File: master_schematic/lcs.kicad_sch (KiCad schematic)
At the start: 6 parts, among them U10 HX711, U11 HX711, U12 LoadCell, U13 HX711, U14 LoadCell, U3 LoadCell

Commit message: minor updates
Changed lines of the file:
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@@
-		)
-	)
-	(bus
-		(pts
-			(xy 67.31 129.54) (xy 67.31 135.89)
-		)
-		(stroke
-			(width 0)
-			(type default)
 		)
 	)

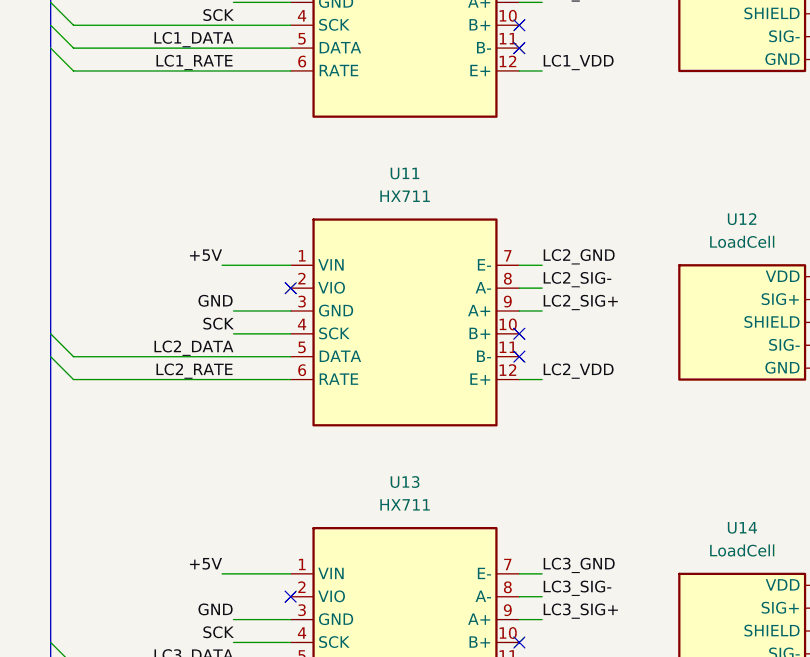
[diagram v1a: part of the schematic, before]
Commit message: updated with part info
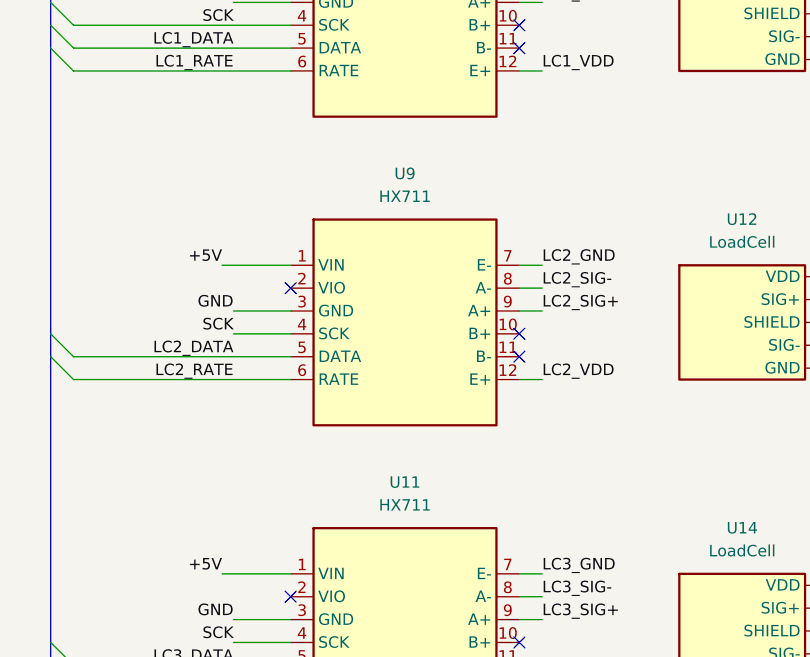
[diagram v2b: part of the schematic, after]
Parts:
- removed U13: HX711, Connector_PinHeader_1.00mm:PinHeader_1x06_P1.00mm_Vertical, symbol hb_symbol_lib:hx711_load_cell_amplifier
- added U9: HX711, hb_footprint_lib:hx711_connector, symbol hb_symbol_lib:hx711_load_cell_amplifier
- U10, U11: footprint Connector_PinHeader_1.00mm:PinHeader_1x06_P1.00mm_Vertical -> hb_footprint_lib:hx711_connector
- U12, U14, U3: now left out of the parts list
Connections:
- net +5V: now also U9.1 (VIN)
- net GND: now also U9.3 (GND)
- net LC2_DATA: now also U9.5 (DATA); no longer U11.5 (DATA)
- net LC2_GND: now also U9.7 (E-); no longer U11.7 (E-)
- net LC2_RATE: now also U9.6 (RATE); no longer U11.6 (RATE)
- net LC2_SIG+: now also U9.9 (A+); no longer U11.9 (A+)
- net LC2_SIG-: now also U9.8 (A-); no longer U11.8 (A-)
- net LC2_VDD: now also U9.12 (E+); no longer U11.12 (E+)
- net LC3_DATA: now also U11.5 (DATA)
- net LC3_GND: now also U11.7 (E-)
- net LC3_RATE: now also U11.6 (RATE)
- net LC3_SIG+: now also U11.9 (A+)
- net LC3_SIG-: now also U11.8 (A-)
- net LC3_VDD: now also U11.12 (E+)
- net SCK: now also U9.4 (SCK)

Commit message: fixed errors on schematic
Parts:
- renumbered U9 to U10, U3 to U12, U12 to U13, U10 to U9
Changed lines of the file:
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@@
 		(dnp no)
 		(fields_autoplaced yes)
-		(property "Reference" "#PWR033"
+		(property "Reference" "#PWR050"
 			(at 201.93 63.5 0)
 			(effects
@@
 		)
 		(instances
-			(project ""
-				(path "/c4f7e98c-e88d-49cc-9841-b70710a90a72/0c2b79c8-c5dd-4fa2-8a84-72fd6742794a"
-					(reference "#PWR033")
+			(project "master_schematic"
+				(path "/c4f7e98c-e88d-49cc-9841-b70710a90a72/0c2b79c8-c5dd-4fa2-8a84-72fd6742794a"
+					(reference "#PWR050")
 					(unit 1)
 				)
@@
 		(dnp no)
 		(fields_autoplaced yes)
-		(property "Reference" "U9"
+		(property "Reference" "U10"
 			(at 106.68 74.93 0)
 			(effects
@@
 			(project "master_schematic"
 				(path "/c4f7e98c-e88d-49cc-9841-b70710a90a72/0c2b79c8-c5dd-4fa2-8a84-72fd6742794a"
-					(reference "U9")
+					(reference "U10")
 					(unit 1)
 				)
@@
 		(dnp no)
 		(fields_autoplaced yes)
-		(property "Reference" "#PWR034"
+		(property "Reference" "#PWR048"
 			(at 187.96 68.58 0)
 			(effects
@@
 			(project "master_schematic"
 				(path "/c4f7e98c-e88d-49cc-9841-b70710a90a72/0c2b79c8-c5dd-4fa2-8a84-72fd6742794a"
-					(reference "#PWR034")
+					(reference "#PWR048")
 					(unit 1)
 				)
@@
 		(dnp no)
 		(fields_autoplaced yes)
-		(property "Reference" "U10"
+		(property "Reference" "U9"
 			(at 106.68 40.64 0)
 			(effects
@@
 		)
 		(instances
-			(project ""
-				(path "/c4f7e98c-e88d-49cc-9841-b70710a90a72/0c2b79c8-c5dd-4fa2-8a84-72fd6742794a"
-					(reference "U10")
+			(project "master_schematic"
+				(path "/c4f7e98c-e88d-49cc-9841-b70710a90a72/0c2b79c8-c5dd-4fa2-8a84-72fd6742794a"
+					(reference "U9")
 					(unit 1)
 				)
@@
 		(dnp no)
 		(fields_autoplaced yes)
-		(property "Reference" "#PWR035"
+		(property "Reference" "#PWR049"
 			(at 195.58 53.34 0)
 			(effects
@@
 			(project "master_schematic"
 				(path "/c4f7e98c-e88d-49cc-9841-b70710a90a72/0c2b79c8-c5dd-4fa2-8a84-72fd6742794a"
-					(reference "#PWR035")
+					(reference "#PWR049")
 					(unit 1)
 				)
@@
 		(dnp no)
 		(fields_autoplaced yes)
-		(property "Reference" "U12"
+		(property "Reference" "U13"
 			(at 144.145 80.01 0)
 			(effects
@@
 			(project "master_schematic"
 				(path "/c4f7e98c-e88d-49cc-9841-b70710a90a72/0c2b79c8-c5dd-4fa2-8a84-72fd6742794a"
-					(reference "U12")
+					(reference "U13")
 					(unit 1)
 				)
@@
 		(dnp no)
 		(fields_autoplaced yes)
-		(property "Reference" "U3"
+		(property "Reference" "U12"
 			(at 144.145 45.72 0)
 			(effects
@@
 		)
 		(instances
-			(project ""
-				(path "/c4f7e98c-e88d-49cc-9841-b70710a90a72/0c2b79c8-c5dd-4fa2-8a84-72fd6742794a"
-					(reference "U3")
-					(unit 1)
-				)
+			(project "master_schematic"
+				(path "/c4f7e98c-e88d-49cc-9841-b70710a90a72/0c2b79c8-c5dd-4fa2-8a84-72fd6742794a"
+					(reference "U12")
+					(unit 1)
+				)

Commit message: patch fix
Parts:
- U10, U11, U9: footprint hb_footprint_lib:hx711_connector -> Connector_PinHeader_1.00mm:PinHeader_1x06_P1.00mm_Vertical
- U12, U13, U14: now not fitted
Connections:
- net LC1_GND: no longer U9.7 (E-)
- net LC1_SIG+: no longer U9.9 (A+)
- net LC1_SIG-: no longer U9.8 (A-)
- net LC1_VDD: no longer U9.12 (E+)
- net LC2_GND: no longer U10.7 (E-)
- net LC2_SIG+: no longer U10.9 (A+)
- net LC2_SIG-: no longer U10.8 (A-)
- net LC2_VDD: no longer U10.12 (E+)
- net LC3_GND: no longer U11.7 (E-)
- net LC3_SIG+: no longer U11.9 (A+)
- net LC3_SIG-: no longer U11.8 (A-)
- net LC3_VDD: no longer U11.12 (E+)
- no-connect marks 9 -> 3

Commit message: finished building PCB
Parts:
- U10, U11, U9: footprint Connector_PinHeader_1.00mm:PinHeader_1x06_P1.00mm_Vertical -> hb_footprint_lib:hx711_connector
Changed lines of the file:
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@@
 	)
 	(symbol
-		(lib_name "hx711_load_cell_amplifier_2")
+		(lib_name "hx711_load_cell_amplifier_1")
 		(lib_id "hb_symbol_lib:hx711_load_cell_amplifier")
-		(at 106.68 91.44 0)
+		(at 106.68 125.73 0)
 		(unit 1)
 		(exclude_from_sim no)
@@
 		(dnp no)
 		(fields_autoplaced yes)
-		(property "Reference" "U10"
-			(at 106.68 74.93 0)
+		(property "Reference" "U11"
+			(at 106.68 109.22 0)
 			(effects
 				(font
@@
 		)
 		(property "Value" "HX711"
-			(at 106.68 77.47 0)
-			(effects
-				(font
-					(size 1.27 1.27)
-				)
-			)
-		)
-		(property "Footprint" "Connector_PinHeader_1.00mm:PinHeader_1x06_P1.00mm_Vertical"
-			(at 105.664 91.44 90)
+			(at 106.68 111.76 0)
+			(effects
+				(font
+					(size 1.27 1.27)
+				)
+			)
+		)
+		(property "Footprint" "hb_footprint_lib:hx711_connector"
+			(at 105.664 125.73 90)
 			(effects
 				(font
@@
 		)
 		(property "Datasheet" "https://learn.adafruit.com/adafruit-hx711-24-bit-adc"
-			(at 106.934 91.44 90)
+			(at 106.934 125.73 90)
 			(effects
 				(font
@@
 		)
 		(property "Description" ""
-			(at 106.934 91.44 90)
+			(at 106.934 125.73 90)
 			(effects
 				(font
@@
 			(project "master_schematic"
 				(path "/c4f7e98c-e88d-49cc-9841-b70710a90a72/0c2b79c8-c5dd-4fa2-8a84-72fd6742794a"
-					(reference "U10")
+					(reference "U11")
 					(unit 1)
 				)
@@
 			)
 		)
-		(property "Footprint" "Connector_PinHeader_1.00mm:PinHeader_1x06_P1.00mm_Vertical"
+		(property "Footprint" "hb_footprint_lib:hx711_connector"
 			(at 105.664 57.15 90)
 			(effects
@@
 	)
 	(symbol
+		(lib_id "hb_symbol_lib:load_cell_yzc516_50kg")
+		(at 143.51 90.17 0)
+		(unit 1)
+		(exclude_from_sim no)
+		(in_bom no)
+		(on_board no)
+		(dnp yes)
+		(fields_autoplaced yes)
+		(property "Reference" "U13"
+			(at 144.145 80.01 0)
+			(effects
+				(font
+					(size 1.27 1.27)
+				)
+			)
+		)
+		(property "Value" "LoadCell"
+			(at 144.145 82.55 0)
+			(effects
+				(font
+					(size 1.27 1.27)
+				)
+			)
+		)
+		(property "Footprint" ""
+			(at 143.51 90.17 0)
+			(effects
+				(font
+					(size 1.27 1.27)
+				)
+				(hide yes)
+			)
+		)
+		(property "Datasheet" ""
+			(at 143.51 90.17 0)
+			(effects
+				(font
+					(size 1.27 1.27)
+				)
+				(hide yes)
+			)
+		)
+		(property "Description" ""
+			(at 143.51 90.17 0)
+			(effects
+				(font
+					(size 1.27 1.27)
+				)
+				(hide yes)
+			)
+		)
+		(pin "5"
+		)
+		(pin "2"
+		)
+		(pin "1"
+		)
+		(pin "3"
+		)
+		(pin "4"
+		)
+		(instances
+			(project "master_schematic"
+				(path "/c4f7e98c-e88d-49cc-9841-b70710a90a72/0c2b79c8-c5dd-4fa2-8a84-72fd6742794a"
+					(reference "U13")
+					(unit 1)
+				)
+			)
+		)
+	)
+	(symbol
+		(lib_id "hb_symbol_lib:load_cell_yzc516_50kg")
+		(at 143.51 55.88 0)
+		(unit 1)
+		(exclude_from_sim no)
+		(in_bom no)
+		(on_board no)
+		(dnp yes)
+		(fields_autoplaced yes)
+		(property "Reference" "U12"
+			(at 144.145 45.72 0)
+			(effects
+				(font
+					(size 1.27 1.27)
+				)
+			)
+		)
+		(property "Value" "LoadCell"
+			(at 144.145 48.26 0)
+			(effects
+				(font
+					(size 1.27 1.27)
+				)
+			)
+		)
+		(property "Footprint" ""
+			(at 143.51 55.88 0)
+			(effects
+				(font
+					(size 1.27 1.27)
+				)
+				(hide yes)
+			)
+		)
+		(property "Datasheet" ""
+			(at 143.51 55.88 0)
+			(effects
+				(font
+					(size 1.27 1.27)
+				)
+				(hide yes)
+			)
+		)
+		(property "Description" ""
+			(at 143.51 55.88 0)
+			(effects
+				(font
+					(size 1.27 1.27)
+				)
+				(hide yes)
+			)
+		)
+		(pin "5"
+		)
+		(pin "2"
+		)
+		(pin "1"
+		)
+		(pin "3"
+		)
+		(pin "4"
+		)
+		(instances
+			(project "master_schematic"
+				(path "/c4f7e98c-e88d-49cc-9841-b70710a90a72/0c2b79c8-c5dd-4fa2-8a84-72fd6742794a"
+					(reference "U12")
+					(unit 1)
+				)
+			)
+		)
+	)
+	(symbol
+		(lib_name "hx711_load_cell_amplifier_1")
 		(lib_id "hb_symbol_lib:hx711_load_cell_amplifier")
-		(at 106.68 125.73 0)
+		(at 106.68 91.44 0)
 		(unit 1)
 		(exclude_from_sim no)
@@
 		(dnp no)
 		(fields_autoplaced yes)
-		(property "Reference" "U11"
-			(at 106.68 109.22 0)
+		(property "Reference" "U10"
+			(at 106.68 74.93 0)
 			(effects
 				(font
@@
 		)
 		(property "Value" "HX711"
-			(at 106.68 111.76 0)
-			(effects
-				(font
-					(size 1.27 1.27)
-				)
-			)
-		)
-		(property "Footprint" "Connector_PinHeader_1.00mm:PinHeader_1x06_P1.00mm_Vertical"
-			(at 105.664 125.73 90)
+			(at 106.68 77.47 0)
+			(effects
+				(font
+					(size 1.27 1.27)
+				)
+			)
+		)
+		(property "Footprint" "hb_footprint_lib:hx711_connector"
+			(at 105.664 91.44 90)
 			(effects
 				(font
@@
 		)
 		(property "Datasheet" "https://learn.adafruit.com/adafruit-hx711-24-bit-adc"
-			(at 106.934 125.73 90)
+			(at 106.934 91.44 90)
 			(effects
 				(font
@@
 		)
 		(property "Description" ""
-			(at 106.934 125.73 90)
+			(at 106.934 91.44 90)
 			(effects
 				(font
@@
 			(project "master_schematic"
 				(path "/c4f7e98c-e88d-49cc-9841-b70710a90a72/0c2b79c8-c5dd-4fa2-8a84-72fd6742794a"
-					(reference "U11")
-					(unit 1)
-				)
-			)
-		)
-	)
-	(symbol
-		(lib_id "hb_symbol_lib:load_cell_yzc516_50kg")
-		(at 143.51 90.17 0)
-		(unit 1)
-		(exclude_from_sim no)
-		(in_bom no)
-		(on_board no)
-		(dnp yes)
-		(fields_autoplaced yes)
-		(property "Reference" "U13"
-			(at 144.145 80.01 0)
-			(effects
-				(font
-					(size 1.27 1.27)
-				)
-			)
-		)
-		(property "Value" "LoadCell"
-			(at 144.145 82.55 0)
-			(effects
-				(font
-					(size 1.27 1.27)
-				)
-			)
-		)
-		(property "Footprint" ""
-			(at 143.51 90.17 0)
-			(effects
-				(font
-					(size 1.27 1.27)
-				)
-				(hide yes)
-			)
-		)
-		(property "Datasheet" ""
-			(at 143.51 90.17 0)
-			(effects
-				(font
-					(size 1.27 1.27)
-				)
-				(hide yes)
-			)
-		)
-		(property "Description" ""
-			(at 143.51 90.17 0)
-			(effects
-				(font
-					(size 1.27 1.27)
-				)
-				(hide yes)
-			)
-		)
-		(pin "5"
-		)
-		(pin "2"
-		)
-		(pin "1"
-		)
-		(pin "3"
-		)
-		(pin "4"
-		)
-		(instances
-			(project "master_schematic"
-				(path "/c4f7e98c-e88d-49cc-9841-b70710a90a72/0c2b79c8-c5dd-4fa2-8a84-72fd6742794a"
-					(reference "U13")
-					(unit 1)
-				)
-			)
-		)
-	)
-	(symbol
-		(lib_id "hb_symbol_lib:load_cell_yzc516_50kg")
-		(at 143.51 55.88 0)
-		(unit 1)
-		(exclude_from_sim no)
-		(in_bom no)
-		(on_board no)
-		(dnp yes)
-		(fields_autoplaced yes)
-		(property "Reference" "U12"
-			(at 144.145 45.72 0)
-			(effects
-				(font
-					(size 1.27 1.27)
-				)
-			)
-		)
-		(property "Value" "LoadCell"
-			(at 144.145 48.26 0)
-			(effects
-				(font
-					(size 1.27 1.27)
-				)
-			)
-		)
-		(property "Footprint" ""
-			(at 143.51 55.88 0)
-			(effects
-				(font
-					(size 1.27 1.27)
-				)
-				(hide yes)
-			)
-		)
-		(property "Datasheet" ""
-			(at 143.51 55.88 0)
-			(effects
-				(font
-					(size 1.27 1.27)
-				)
-				(hide yes)
-			)
-		)
-		(property "Description" ""
-			(at 143.51 55.88 0)
-			(effects
-				(font
-					(size 1.27 1.27)
-				)
-				(hide yes)
-			)
-		)
-		(pin "5"
-		)
-		(pin "2"
-		)
-		(pin "1"
-		)
-		(pin "3"
-		)
-		(pin "4"
-		)
-		(instances
-			(project "master_schematic"
-				(path "/c4f7e98c-e88d-49cc-9841-b70710a90a72/0c2b79c8-c5dd-4fa2-8a84-72fd6742794a"
-					(reference "U12")
-					(unit 1)
-				)
+					(reference "U10")
+					(unit 1)
+				)

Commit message: updated BOM
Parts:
- U10, U11, U9: Cost @ Qty (none) -> 0.47; Manufacturer (none) -> Sullins Connector Solutions; Manufacturer Part # (none) -> PPPC061LFBN-RC; Supplier (none) -> Digikey; Supplier Part # (none) -> PPPC061LFBN-RC; Unit Cost (none) -> 0.47

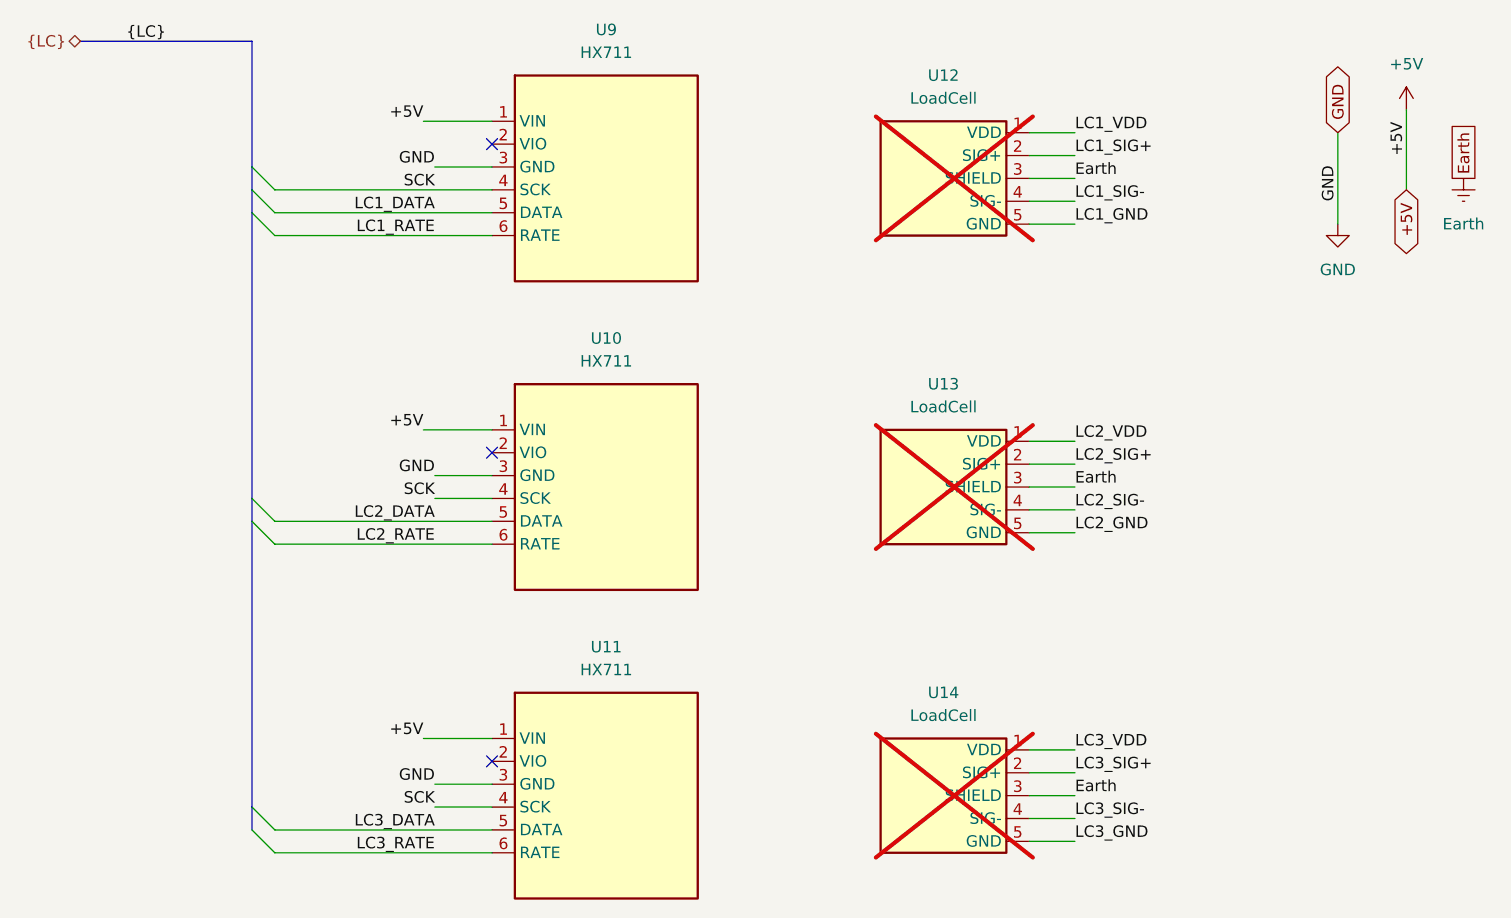
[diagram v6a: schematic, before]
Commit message: added decoupling capacitors, fixed voltage values for TTs and load cells to +3V3
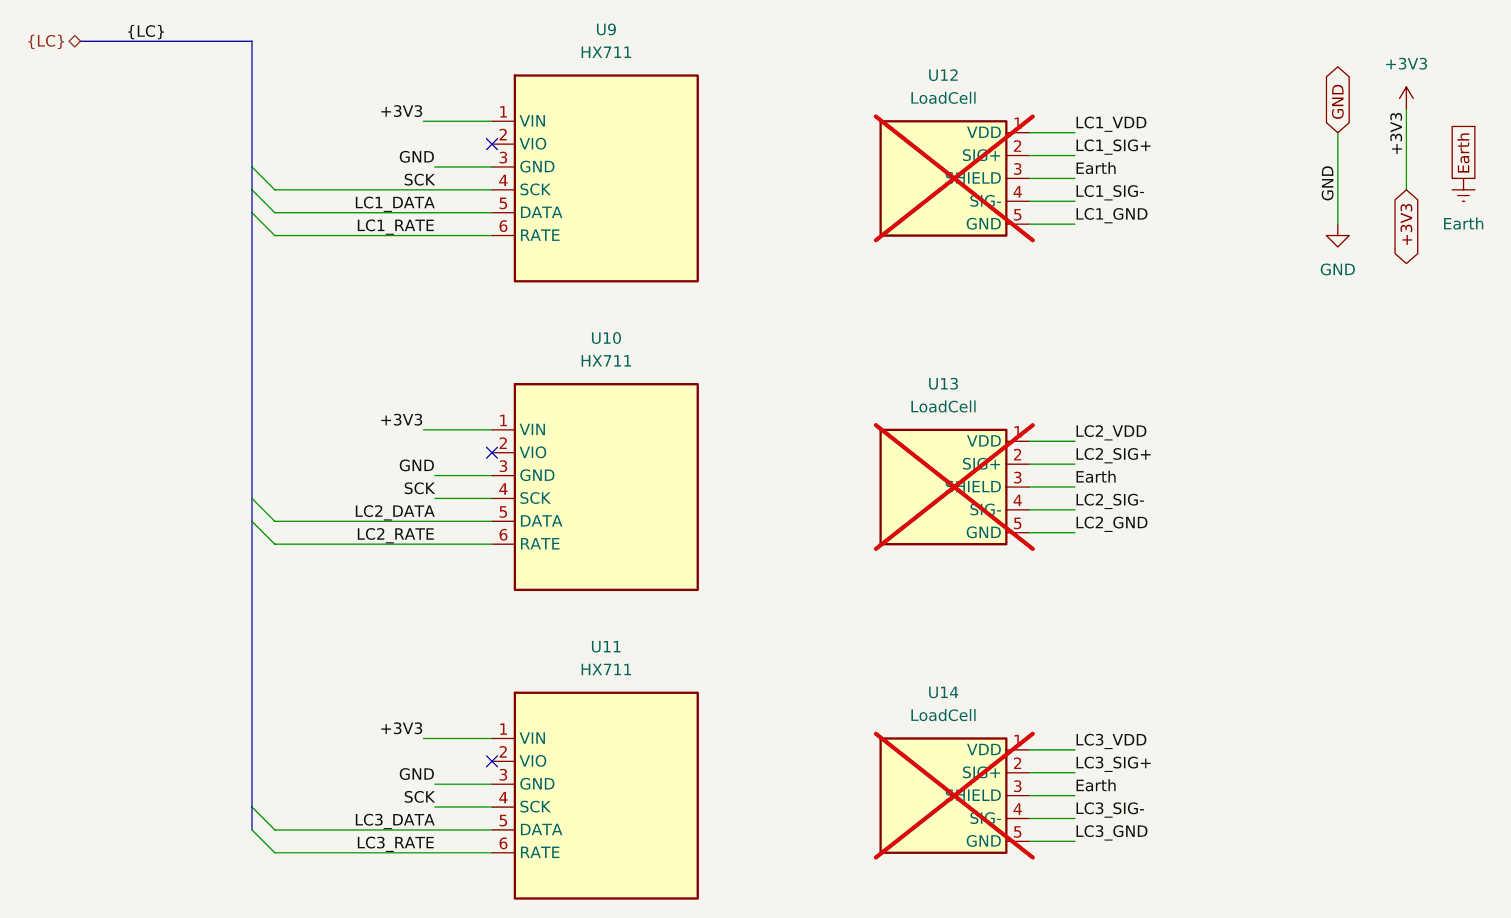
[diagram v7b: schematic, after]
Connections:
- net +5V renamed +3V3
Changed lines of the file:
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@@
 		)
 	)
-	(label "+5V"
+	(label "+3V3"
 		(at 86.36 119.38 180)
 		(fields_autoplaced yes)
@@
 		)
 	)
-	(label "+5V"
+	(label "+3V3"
 		(at 86.36 85.09 180)
 		(fields_autoplaced yes)
@@
 		)
 	)
-	(label "+5V"
+	(label "+3V3"
 		(at 195.58 54.61 90)
 		(fields_autoplaced yes)
@@
 		)
 	)
-	(label "+5V"
+	(label "+3V3"
 		(at 86.36 50.8 180)
 		(fields_autoplaced yes)
@@
 		)
 	)
-	(global_label "+5V"
+	(global_label "+3V3"
 		(shape bidirectional)
 		(at 195.58 58.42 270)
@@
 		(dnp no)
 		(fields_autoplaced yes)
-		(property "Reference" "#PWR050"
+		(property "Reference" "#PWR065"
 			(at 201.93 63.5 0)
 			(effects
@@
 			(project "master_schematic"
 				(path "/c4f7e98c-e88d-49cc-9841-b70710a90a72/0c2b79c8-c5dd-4fa2-8a84-72fd6742794a"
-					(reference "#PWR050")
+					(reference "#PWR065")
 					(unit 1)
 				)
@@
 		(dnp no)
 		(fields_autoplaced yes)
-		(property "Reference" "#PWR048"
+		(property "Reference" "#PWR063"
 			(at 187.96 68.58 0)
 			(effects
@@
 			(project "master_schematic"
 				(path "/c4f7e98c-e88d-49cc-9841-b70710a90a72/0c2b79c8-c5dd-4fa2-8a84-72fd6742794a"
-					(reference "#PWR048")
+					(reference "#PWR063")
 					(unit 1)
 				)
@@
 		(dnp no)
 		(fields_autoplaced yes)
-		(property "Reference" "#PWR049"
+		(property "Reference" "#PWR064"
 			(at 195.58 53.34 0)
 			(effects
@@
 			)
 		)
-		(property "Value" "+5V"
+		(property "Value" "+3V3"
 			(at 195.58 44.45 0)
 			(effects
@@
 			(project "master_schematic"
 				(path "/c4f7e98c-e88d-49cc-9841-b70710a90a72/0c2b79c8-c5dd-4fa2-8a84-72fd6742794a"
-					(reference "#PWR049")
+					(reference "#PWR064")
 					(unit 1)
 				)
